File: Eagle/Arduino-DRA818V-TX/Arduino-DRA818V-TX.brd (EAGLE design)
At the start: 68.6 x 53.3 mm, 23 parts, among them M1 ARDUINO_R3_ICSP, X1 SMA, X2 SMA

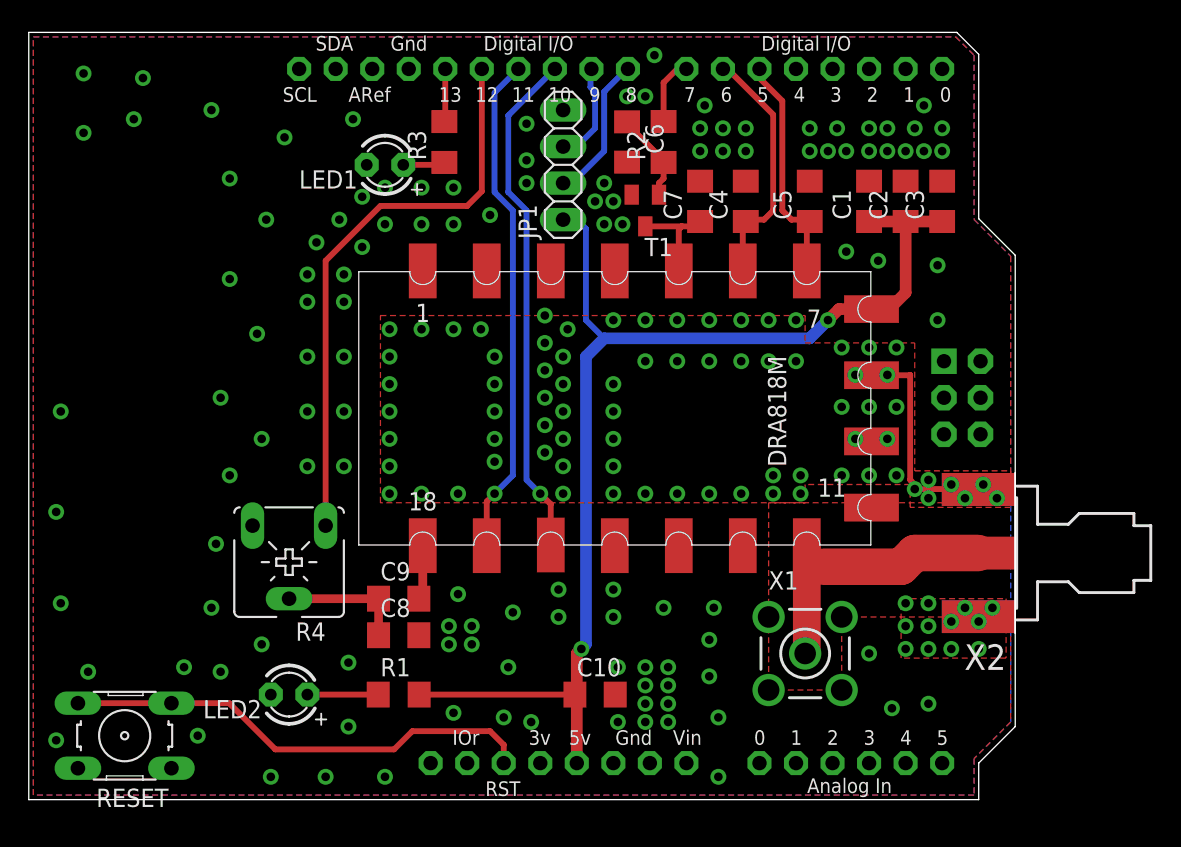
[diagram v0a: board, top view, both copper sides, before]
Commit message: Adding Dorji Library
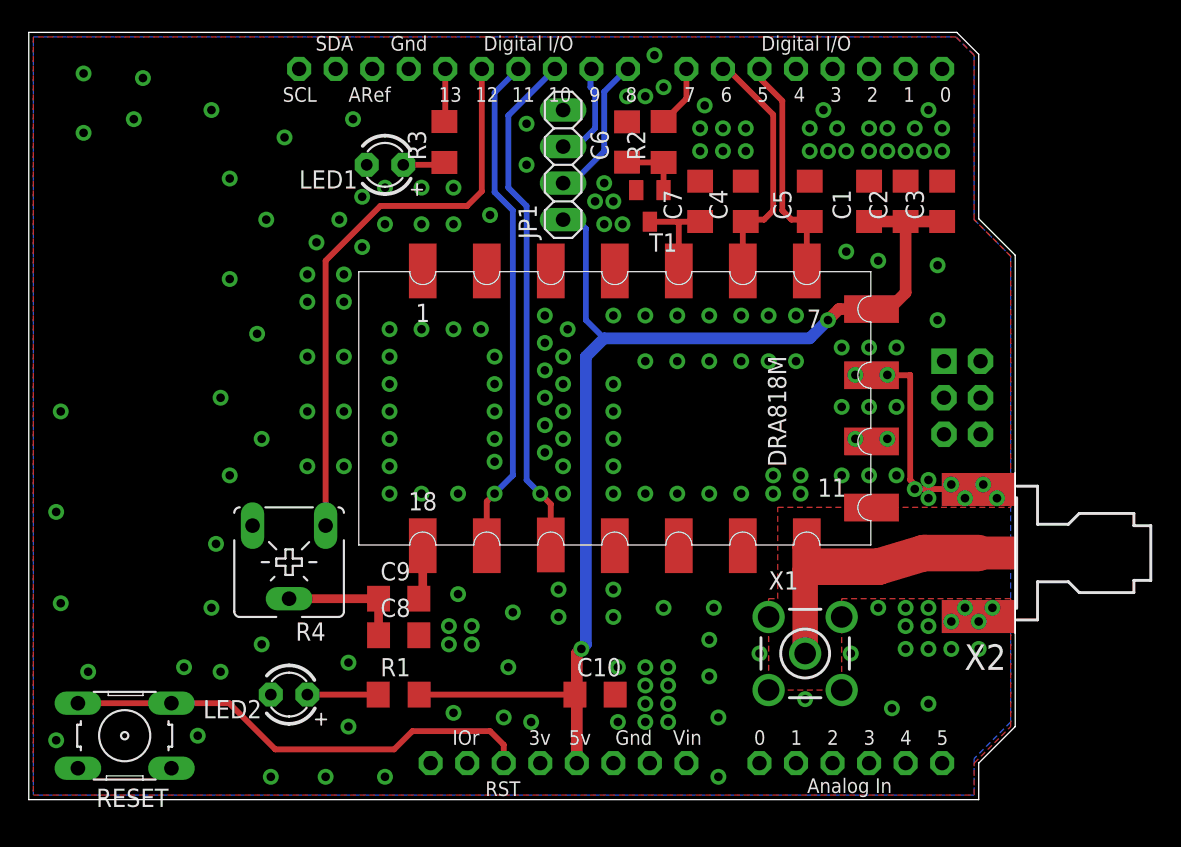
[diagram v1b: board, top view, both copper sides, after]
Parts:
- C10: value 1n -> 1u
- moved T1 0.45 mm to (57.8, 73.0)
- turned C6 to 90 degrees
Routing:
- net N$7: track 6.25 -> 4.49 mm
- net GND: vias 209 -> 213
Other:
- board text removed: "HANDIKO - YD1SDL"
